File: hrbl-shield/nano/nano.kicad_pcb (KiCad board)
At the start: 2 copper layers, 79.8 x 140.1 mm, 65 parts, among them P1 Digital, P2 Analog, U1 SFH6206-3T, U10 SFH6206-3T, U11 SFH6206-3T, U12 SFH6206-3T, U13 SFH6206-3T, U14 SFH6206-3T, U15 IFX27001TFV50ATMA1CT-ND, U16 SFH6206-3T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

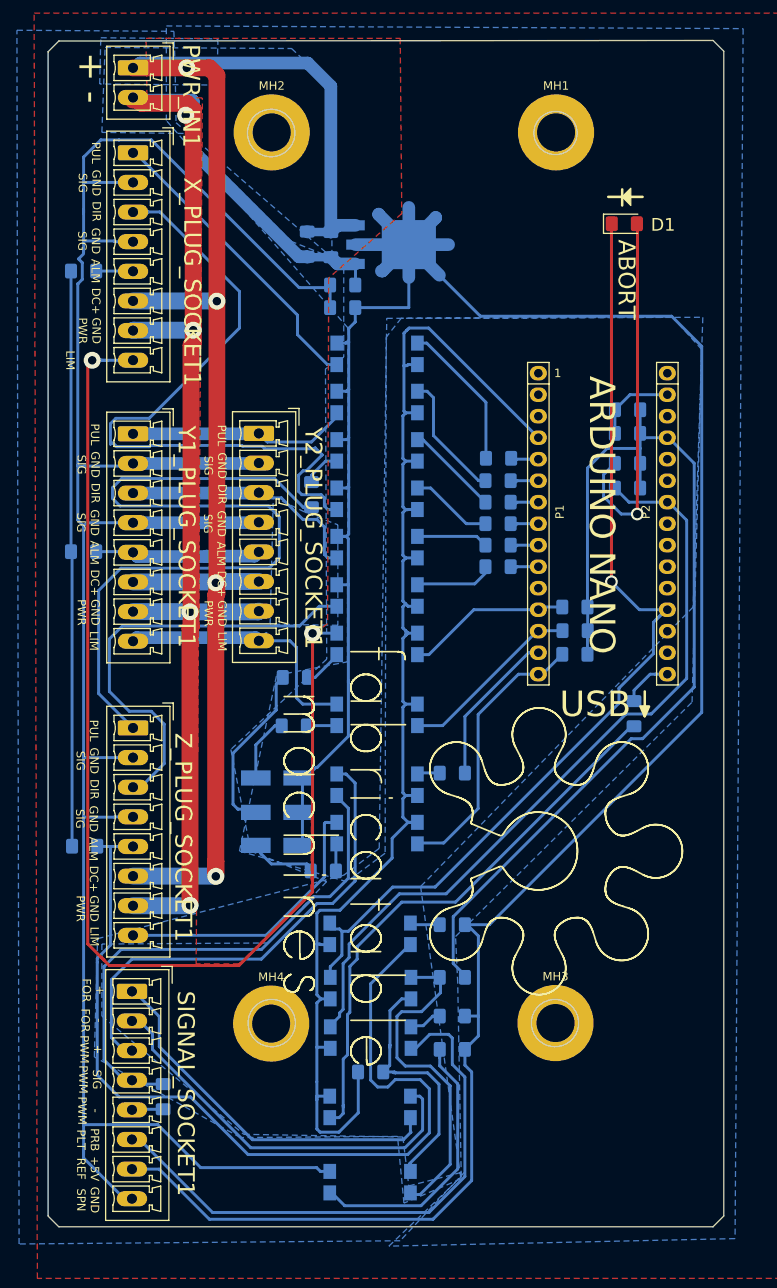
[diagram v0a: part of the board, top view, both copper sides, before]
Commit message: Added spindle fault Abort to old card
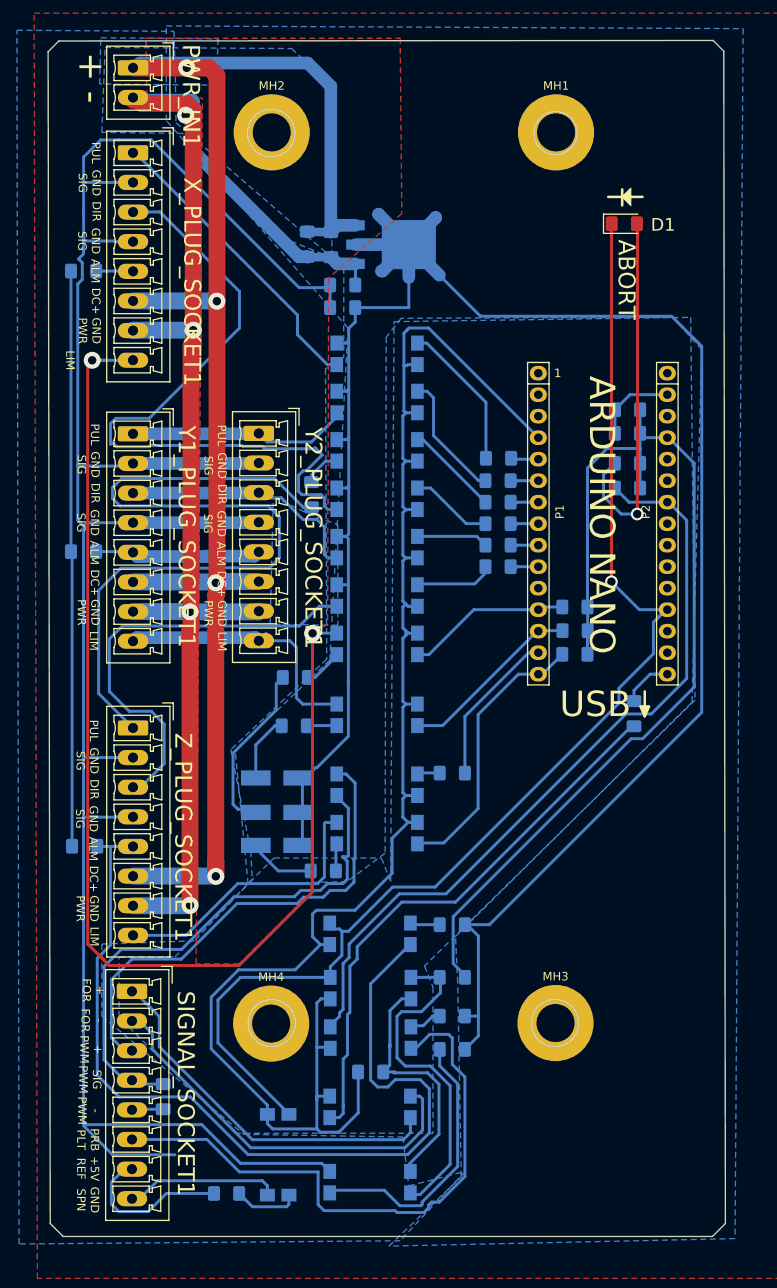
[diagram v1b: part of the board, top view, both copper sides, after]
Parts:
- removed REF**: fabricatable_machines, Symbol:Fabricatable_machines_logo
- added R28: 220, Resistor_SMD:R_1206_3216Metric_Pad1.42x1.75mm_HandSolder, B.Cu at (102.6, 168.1)
- added U17: SFH6206-3T, Package_DIP:SMDIP-4_W9.53mm_Clearance8mm, B.Cu at (108.7, 163.6)
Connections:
- SIGNAL_SOCKET1 pad 7: 5V_ISO -> EXTRA_ALARM_1
- SIGNAL_SOCKET1 pad 8: GNDS -> EXTRA_ALARM_2
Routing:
- net 5V_ISO: track 319.3 -> 249.9 mm
- net GND: track 196.6 -> 230.7 mm
- net ABORT: track 117.7 -> 149.1 mm
- net EXTRA_ALARM_2: track 0.00 -> 19.1 mm
- net EXTRA_ALARM_1: track 0.00 -> 19.0 mm
- net Net-(R28-Pad1): track 0.00 -> 7.74 mm
- net PROBE_PLATE: track 67.4 -> 69.8 mm
- net SIGNAL_SPEED: track 63.4 -> 64.1 mm
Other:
- board size 79.8 x 140.1 mm -> 80 x 141.3 mm

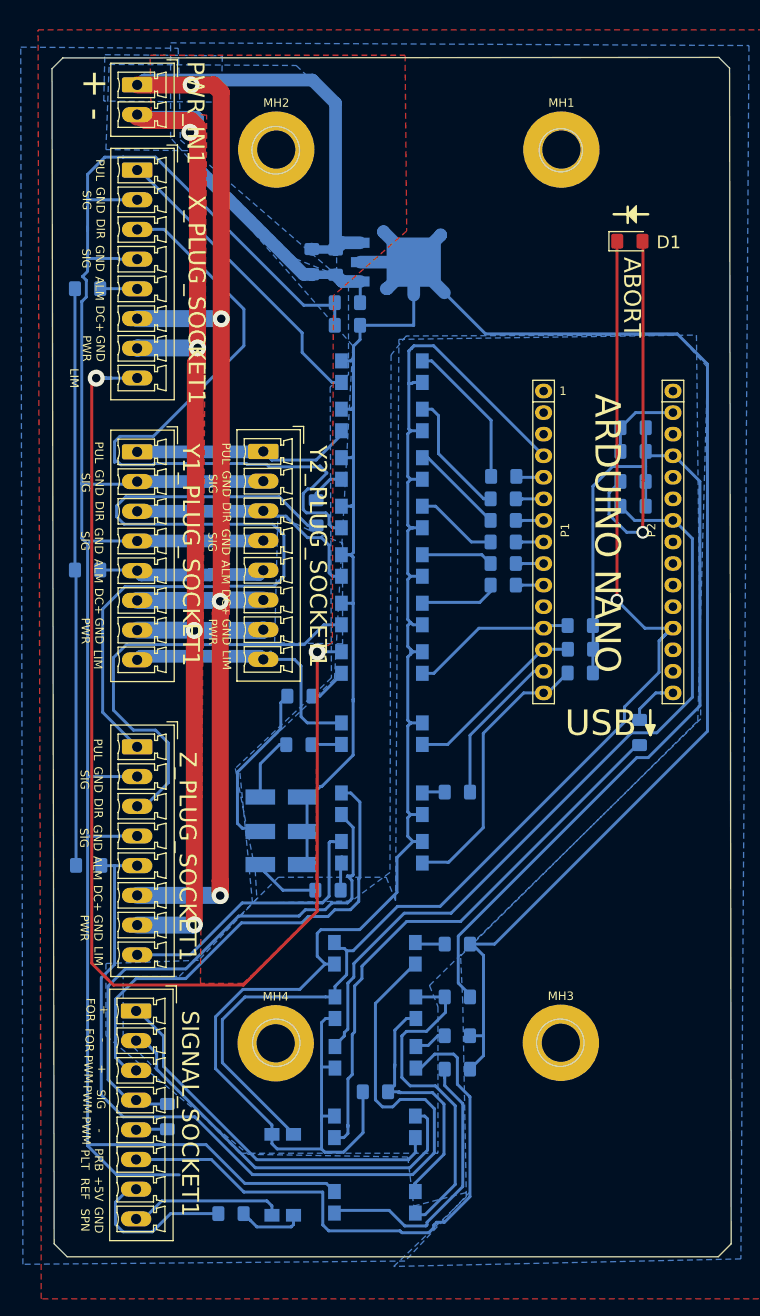
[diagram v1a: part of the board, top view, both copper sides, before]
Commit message: Added serial pins and more noise protection
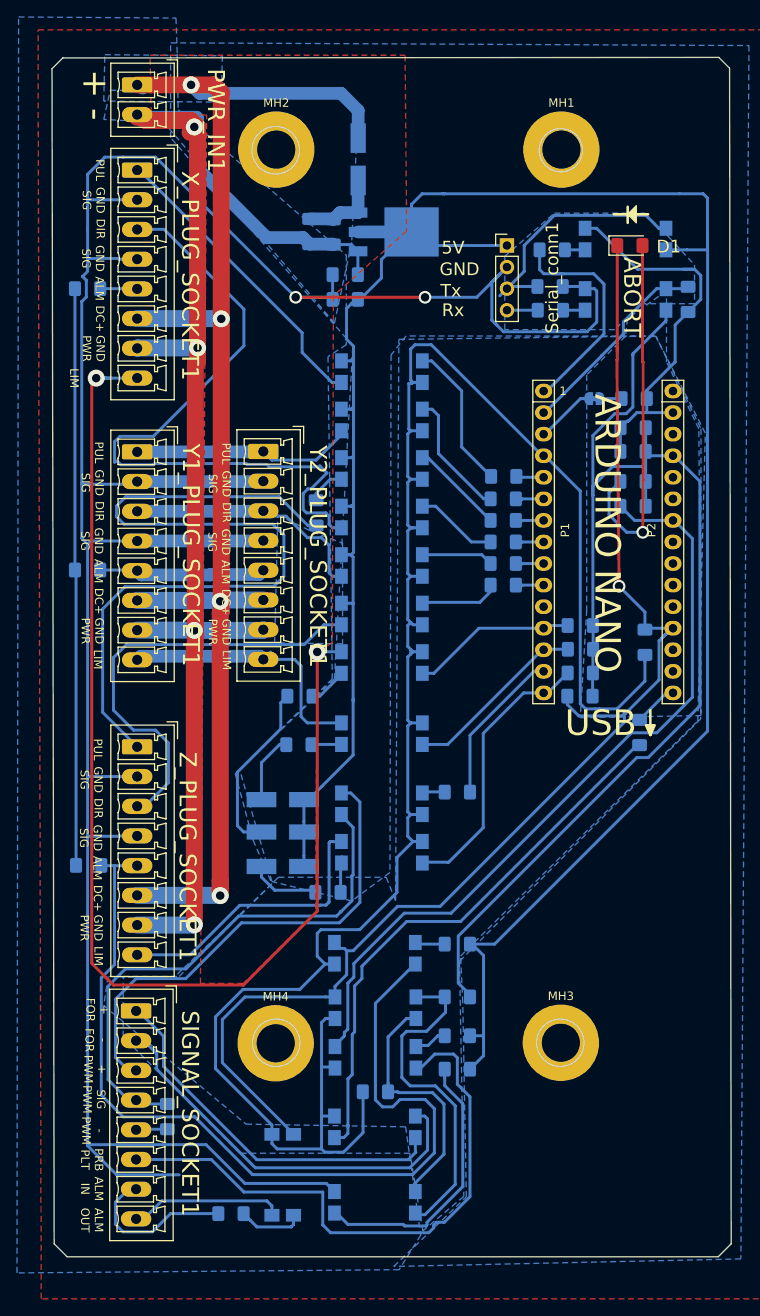
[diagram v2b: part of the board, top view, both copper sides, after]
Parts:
- removed S1JA-13-F1, S1JA-13-F2, S1JA-13-F3: DIODE, Diode_SMD:D_SMA_Handsoldering
- added C4: 10uF, Capacitor_SMD:C_1206_3216Metric_Pad1.42x1.75mm_HandSolder, B.Cu at (150.1, 72.1)
- added C7: 0.1uF, Capacitor_SMD:C_1206_3216Metric_Pad1.42x1.75mm_HandSolder, B.Cu at (151.4, 100.8)
- added D2->|-1: 1N4007, Diode_SMD:D_SMA_Handsoldering, B.Cu at (117.6, 43.9)
- added D3->|-1: 1N4007, Diode_SMD:D_SMA_Handsoldering, B.Cu at (108.7, 123.2)
- added D4->|-1: 1N4007, Diode_SMD:D_SMA_Handsoldering, B.Cu at (108.7, 119.4)
- added D5->|-1: 1N4007, Diode_SMD:D_SMA_Handsoldering, B.Cu at (108.7, 127.3)
- added R29: 220, Resistor_SMD:R_1206_3216Metric_Pad1.42x1.75mm_HandSolder, B.Cu at (140.2, 61.7)
- added R30: 1k, Resistor_SMD:R_1206_3216Metric_Pad1.42x1.75mm_HandSolder, B.Cu at (156.5, 60.5)
- added R31: 1k, Resistor_SMD:R_1206_3216Metric_Pad1.42x1.75mm_HandSolder, B.Cu at (143.7, 107.2)
- added R32: 220, Resistor_SMD:R_1206_3216Metric_Pad1.42x1.75mm_HandSolder, B.Cu at (140.5, 54.6)
- added R33: 1k, Resistor_SMD:R_1206_3216Metric_Pad1.42x1.75mm_HandSolder, B.Cu at (140.2, 58.9)
- added RESET_CAP_JUMPER1: ~, Jumper:SolderJumper-2_P1.3mm_Bridged_RoundedPad1.0x1.5mm, B.Cu at (145.4, 72.1)
- added Serial_conn1: Conn_01x04, Connector_PinHeader_2.54mm:PinHeader_1x04_P2.54mm_Vertical, F.Cu at (135.1, 54.1)
- added U18: SFH6206-3T, Package_DIP:SMDIP-4_W9.53mm_Clearance8mm, B.Cu at (149.1, 60.5)
- added U19: SFH6206-3T, Package_DIP:SMDIP-4_W9.53mm_Clearance8mm, B.Cu at (149.1, 53.3)
- C2: value 100nF (0.1uF) -> 0.1uF
- C3: value 100nF -> 0.1uF
- D1: value LED -> LED (20mA 1.85V)
- R23, R24, R25, R26, R27: value 1000 -> 1k
- moved C2 3.57 mm to (114.7, 52.5)
- moved U15 3.57 mm to (121.8, 52.5)
- moved C5 3.57 mm to (111.9, 52.5)
- moved R20 3.31 mm to (116.1, 57.5)
- moved C1 3.06 mm to (116.1, 60.5)
- moved D1 0.51 mm to (149.6, 54.1)
- moved R4 0.25 mm to (114.0, 130.3)
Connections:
- net EXTRA_ALARM_1 renamed EXTRA_ALARM_IN
- net EXTRA_ALARM_2 renamed EXTRA_ALARM_OUT
- C2 pad 1: +36V -> Net-(C2-Pad1)
- C5 pad 1: +36V -> Net-(C2-Pad1)
- P1 pad 1: (no net) -> Tx
- P1 pad 2: (no net) -> Rx
- P1 pad 3: /Reset -> RESET
- P2 pad 3: /Reset -> (no net)
- U15 pad 3: +36V -> Net-(C2-Pad1)
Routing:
- net GND: track 230.7 -> 309.1 mm
- net GNDS: track 266.5 -> 321.7 mm, vias 0 -> 2
- net Tx_conn: track 0.00 -> 29.9 mm
- net +5V: track 120.1 -> 149.1 mm
- net Tx: track 0.00 -> 27.4 mm
- net Rx: track 0.00 -> 23.7 mm
- net +36V: track 188.8 -> 165.7 mm
- net 5V_ISO: track 249.9 -> 271.9 mm
- net Net-(C2-Pad1): track 0.00 -> 9.84 mm
- net ABORT: track 149.1 -> 157.2 mm
- net RESET: track 0.00 -> 7.07 mm
- net Rx_conn: track 0.00 -> 4.35 mm
- net Net-(R32-Pad1): track 0.00 -> 2.64 mm
- net Net-(R29-Pad1): track 0.00 -> 2.60 mm
- net Net-(C4-Pad2): track 0.00 -> 2.32 mm
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- added copper zone on B.Cu, net +5V
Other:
- board text added: "5V"
- board text added: "ALM IN"
- board text added: "ALM OUT"
- board text added: "GND"
- board text added: "Rx"
- board text added: "Tx"
- board text removed: "+5V REF"
- board text removed: "-|<-"
- board text removed: "1K"
- board text removed: "GND SPN"

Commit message: JLCPCB test files and added logo
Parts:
- added REF**: Fabricatable_machines, Fabricatable_machines_symbols:Fabricatable_machines, F.Cu at (136.9, 127.5)
- turned MH3 to 90 degrees

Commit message: Lots of JLCPCB tests
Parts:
- removed REF**: Fabricatable_machines, Fabricatable_machines_symbols:Fabricatable_machines
- D1: footprint LED_SMD:LED_1206_3216Metric_Pad1.42x1.75mm_HandSolder -> LED_THT:LED_D5.0mm
- moved D1 155.5 mm to (35.3, -51.3)
- moved C3 150.6 mm to (32.3, -18.4)
- moved C4 150.6 mm to (32.4, -21.8)
- moved C5 150.6 mm to (-5.84, -41.5)
- moved C6 150.6 mm to (32.2, -15.6)
- moved C7 150.6 mm to (33.7, 6.86)
- moved D5 150.6 mm to (-9.02, 33.3)
- moved MH1 150.6 mm to (23.8, -51.2)
- moved MH3 150.6 mm to (23.7, 54.0)
- moved P1 150.6 mm to (21.7, -22.7)
- moved P2 150.6 mm to (37.0, -22.7)
- moved PWR_IN1 150.6 mm to (-26.2, -58.8)
- moved R1 150.6 mm to (17.0, -12.7)
- moved R10 150.6 mm to (33.0, 17.5)
- moved R11 150.6 mm to (11.6, 24.5)
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- renumbered D2->|-1 to D2, D3->|-1 to D3, D4->|-1 to D4, D5->|-1 to D5
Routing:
- net ABORT: track 157.2 -> 170.9 mm
- net Net-(D1-Pad2): track 43.6 -> 56.6 mm
- net +36V: track 165.7 -> 171.7 mm, vias 4 -> 9
- net GNDPWR: track 173.1 -> 176.1 mm, vias 4 -> 9
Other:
- board text removed: "Cut and patch grounds"

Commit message: more jlcpcb testing
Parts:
- moved C1 105.3 mm to (56.9, 54.0)
- moved C2 105.3 mm to (55.5, 46.0)
- moved C4 105.3 mm to (90.9, 65.7)
- moved D2 105.3 mm to (58.4, 37.5)
- moved D4 105.3 mm to (49.5, 112.9)
- moved MH3 105.3 mm to (82.3, 141.5)
- moved P2 105.3 mm to (95.5, 64.8)
- moved R14 105.3 mm to (70.1, 140.7)
- moved R15 105.3 mm to (70.1, 136.1)
- moved R18 105.3 mm to (26.7, 120.7)
- moved R20 105.3 mm to (56.9, 51.1)
- moved R25 105.3 mm to (84.6, 98.0)
- moved R26 105.3 mm to (90.8, 78.3)
- moved R27 105.3 mm to (35.9, 150.2)
- moved R3 105.3 mm to (51.4, 106.4)
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
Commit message: jlcpcb  ordered
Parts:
- R27, R30, R33: value 1k -> 10k
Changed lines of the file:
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@@
     (44 Edge.Cuts user hide)
     (45 Margin user hide)
-    (46 B.CrtYd user)
+    (46 B.CrtYd user hide)
     (47 F.CrtYd user hide)
     (48 B.Fab user hide)
@@
       (drillshape 0)
       (scaleselection 1)
-      (outputdirectory "./"))
+      (outputdirectory "19112019/"))
   )
   (net 0 "")
@@
       (effects (font (size 1.5 1.5) (thickness 0.3)) (justify mirror))
     )
-    (fp_text value 1k (at -3.302 2.032 180) (layer B.SilkS)
+    (fp_text value 10k (at -3.302 2.032 180) (layer B.SilkS)
       (effects (font (size 1.5 1.5) (thickness 0.3)) (justify mirror))
     )
@@
       (effects (font (size 1.5 1.5) (thickness 0.3)) (justify mirror))
     )
-    (fp_text value 1k (at -4.064 -0.254 90) (layer B.SilkS)
+    (fp_text value 10k (at -4.064 -0.254 90) (layer B.SilkS)
       (effects (font (size 1.5 1.5) (thickness 0.3)) (justify mirror))
     )
@@
       (effects (font (size 2 2) (thickness 0.3)) (justify mirror))
     )
-    (fp_text value 1k (at 4.064 0.127 90) (layer B.SilkS)
-      (effects (font (size 1.5 1.5) (thickness 0.3)) (justify mirror))
-    )
+    (fp_text value 10k (at 4.064 0.127 90) (layer B.SilkS)
+      (effects (font (size 1.5 1.5) (thickness 0.3)) (justify mirror))
+    )
